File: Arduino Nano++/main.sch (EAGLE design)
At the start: 68 parts, among them IC1 LM358N, Q1 IRF9530, Q2 IRF9530

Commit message: Nano++ schematic; guitar hero redo to not use 1/64th bit
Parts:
- removed 10K, 3.9K, 7.68K: (no value), rcl:R-US_0204/7
- removed ANALOG: (no value), con-lsta:FE08-1
- removed D23, D24, D25: BZX90, diode:BZX90
- removed F21, F22: FUSETE5, fuse:FUSETE5
- added D3: BZX90, diode:BZX90
- added R10: 1k, rcl:R-US_0204/7
- added R8, R9: 300, rcl:R-US_0204/7
- added SV3: (no value), con-lsta:FE06-1
- R2: value 10k -> (none)
- R3: value 300 -> (none)
- R5: value 300 -> 10k
- R6: value 1k -> (none)
- renumbered 7.68K1 to R7, D26 to D2, DC_JACK to J1, DIGITAL_0 to SV5, DIGITAL_1 to SV4, NANO_LEFT to SV6, NANO_RIGHT to SV7, POWER to SV2, VREG to SV1
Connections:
- removed net A6: D20.C, F17.1, SV6.10
- removed net A6': ANALOG.2, F17.2
- removed net A7: D21.C, F18.1, SV6.11
- removed net A7': ANALOG.1, F18.2
- removed net N$1: SV2.8
- net 3V3: now also R5.2; no longer R4.2
- net 3V3': now also R6.2; no longer 3.9K.2
- net 3V3EN: now also R9.2; no longer R5.2
- net 5V: now also R3.1, R4.2; no longer R1.1, R2.2
- net 5V': now also R1.2; no longer 10K.2
- net 5VEN: now also R8.2; no longer R3.2
- net A0: now also D5.C, F3.1; no longer D25.C, F22.1
- net A0': now also F3.2, SV3.6; no longer ANALOG.8, F22.2
- net A1: now also D8.C, F6.1; no longer D24.C, F21.1
- net A1': now also F6.2, SV3.5; no longer ANALOG.7, F21.2
- net A2: now also D11.C, F9.1; no longer D23.C, F20.1
- net A2': now also F9.2, SV3.4; no longer ANALOG.6, F20.2
- net A3: now also D14.C, F12.1; no longer D22.C, F19.1
- net A3': now also F12.2, SV3.3; no longer ANALOG.5, F19.2
- net A4: now also D17.C; no longer D18.C
- net A4': now also SV3.2; no longer ANALOG.4
- net A5: now also D20.C, F18.1; no longer D19.C, F16.1
- net A5': now also F18.2, SV3.1; no longer ANALOG.3, F16.2
- net D0: now also D3.C, F1.1; no longer D11.C, F7.1
- net D0': now also F1.2; no longer F7.2
- net D1: now also D6.C, F4.1; no longer D10.C, F6.1
- net D1': now also F4.2; no longer F6.2
- net D10: now also D10.C, F8.1; no longer D15.C, F12.1
- net D10': now also F8.2; no longer F12.2
- net D11: now also D13.C; no longer D14.C
- net D12: now also D16.C, F14.1; no longer D12.C, F9.1
- net D12': now also F14.2; no longer F9.2
- net D13: now also D19.C, F17.1; no longer D13.C, F10.1
- net D13': now also F17.2; no longer F10.2
- net D2: now also F7.1; no longer F5.1
- net D2': now also F7.2; no longer F5.2
- net D3: now also D12.C, F10.1; no longer D8.C, F4.1
- net D3': now also F10.2; no longer F4.2
- net D4: now also D15.C, F13.1; no longer D5.C, F8.1
- net D4': now also F13.2; no longer F8.2
- net D5: now also D18.C, F16.1; no longer D4.C, F1.1
- net D5': now also F16.2; no longer F1.2
- net D6: now also D21.C, F19.1; no longer D6.C, F2.1
- net D6': now also F19.2; no longer F2.2
- net D7: now also D22.C, F20.1; no longer D7.C, F3.1
- net D7': now also F20.2; no longer F3.2
- net D8: now also D4.C, F2.1; no longer D17.C, F14.1
- net D8': now also F2.2; no longer F14.2
- net D9: now also D7.C, F5.1; no longer D16.C, F13.1
- net D9': now also F5.2; no longer F13.2
- net GND: now also D3.A, R2.1; no longer 7.68K.1, D23.A, D24.A, D25.A
- net N$3: now also R9.1; no longer R4.1
- net N$4: now also R4.1, R8.1; no longer R2.1, R3.1
- net N$6: now also R1.1, R2.2; no longer 10K.1, 7.68K.2
- net N$7: now also R6.1; no longer 3.9K.1
- net RST: now also R10.2; no longer R6.2
- net RST': now also R10.1; no longer R6.1
- net VIN: now also SV6.15
- net VREF2.4: now also R3.2; no longer R1.2
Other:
- moved on the sheet: D10, D11, D12, D13, D14, D15, D16, D17, D18, D19, D20, D21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

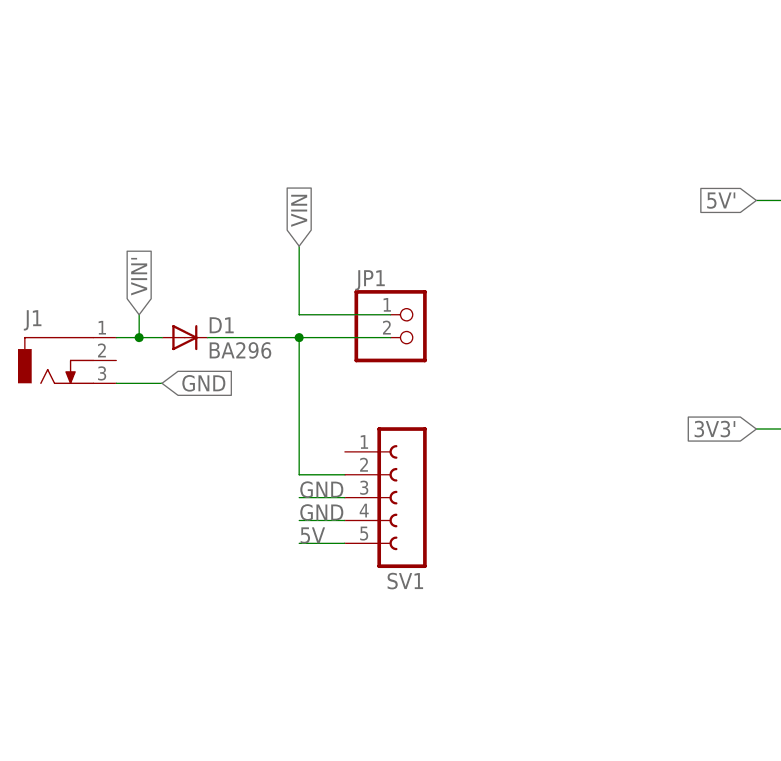
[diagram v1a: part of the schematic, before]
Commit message: Removed vreg slot
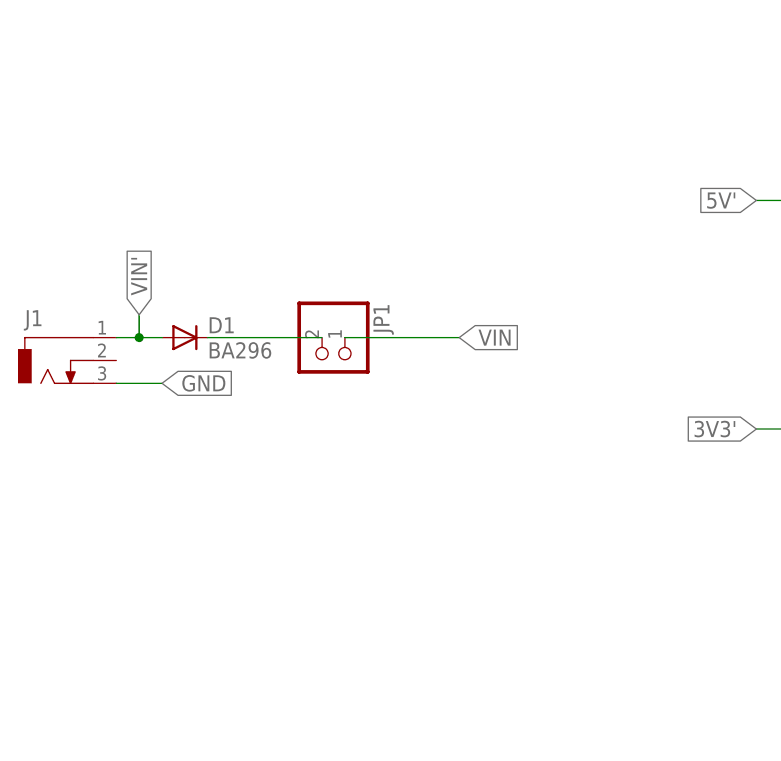
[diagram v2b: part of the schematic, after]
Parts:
- removed SV1: (no value), con-lsta:FE05-1
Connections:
- net 5V: no longer SV1.5
- net GND: no longer SV1.3, SV1.4
- net N$2: no longer SV1.2
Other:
- moved on the sheet: JP1
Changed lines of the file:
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@@
 <part name="SV4" library="con-lsta" library_urn="urn:adsk.eagle:library:161" deviceset="FE08-1" device="" package3d_urn="urn:adsk.eagle:package:8194/1"/>
 <part name="J1" library="con-jack" library_urn="urn:adsk.eagle:library:154" deviceset="DCJ0303" device="" package3d_urn="urn:adsk.eagle:package:7493/1"/>
-<part name="SV1" library="con-lsta" library_urn="urn:adsk.eagle:library:161" deviceset="FE05-1" device="" package3d_urn="urn:adsk.eagle:package:8190/1"/>
 <part name="F13" library="fuse" library_urn="urn:adsk.eagle:library:233" deviceset="FUSE" device="TE5" package3d_urn="urn:adsk.eagle:package:14069/1"/>
 <part name="D15" library="diode" library_urn="urn:adsk.eagle:library:210" deviceset="BZX90" device="" package3d_urn="urn:adsk.eagle:package:43364/1"/>
@@
 <instance part="SV4" gate="G$1" x="121.92" y="25.4" rot="R180"/>
 <instance part="J1" gate="G$1" x="-154.94" y="-40.64"/>
-<instance part="SV1" gate="G$1" x="-114.3" y="-55.88" rot="R180"/>
 <instance part="F13" gate="G$1" x="109.22" y="-55.88" rot="R90"/>
 <instance part="D15" gate="1" x="109.22" y="-68.58" rot="R90"/>
@@
 <instance part="GND4" gate="1" x="-58.42" y="-165.1"/>
 <instance part="D1" gate="1" x="-139.7" y="-38.1"/>
-<instance part="JP1" gate="G$1" x="-114.3" y="-38.1"/>
+<instance part="JP1" gate="G$1" x="-124.46" y="-40.64" rot="R270"/>
 <instance part="R10" gate="G$1" x="-35.56" y="-96.52"/>
 <instance part="SV3" gate="G$1" x="81.28" y="-5.08"/>
@@
 </segment>
 <segment>
-<pinref part="SV1" gate="G$1" pin="5"/>
-<wire x1="-121.92" y1="-60.96" x2="-127" y2="-60.96" width="0.1524" layer="91"/>
-<label x="-127" y="-60.96" size="1.778" layer="95"/>
-</segment>
-<segment>
 <pinref part="IC1" gate="P" pin="V+"/>
 <wire x1="-81.28" y1="-93.98" x2="-81.28" y2="-91.44" width="0.1524" layer="91"/>
@@
 <wire x1="-147.32" y1="-43.18" x2="-142.24" y2="-43.18" width="0.1524" layer="91"/>
 <label x="-142.24" y="-43.18" size="1.778" layer="95" xref="yes"/>
-</segment>
-<segment>
-<pinref part="SV1" gate="G$1" pin="3"/>
-<wire x1="-121.92" y1="-55.88" x2="-127" y2="-55.88" width="0.1524" layer="91"/>
-<label x="-127" y="-55.88" size="1.778" layer="95"/>
-</segment>
-<segment>
-<pinref part="SV1" gate="G$1" pin="4"/>
-<wire x1="-121.92" y1="-58.42" x2="-127" y2="-58.42" width="0.1524" layer="91"/>
-<label x="-127" y="-58.42" size="1.778" layer="95"/>
 </segment>
 </net>
@@
 <segment>
 <pinref part="D1" gate="1" pin="C"/>
-<wire x1="-137.16" y1="-38.1" x2="-127" y2="-38.1" width="0.1524" layer="91"/>
 <pinref part="JP1" gate="G$1" pin="2"/>
-<wire x1="-127" y1="-38.1" x2="-116.84" y2="-38.1" width="0.1524" layer="91"/>
-<junction x="-127" y="-38.1"/>
-<wire x1="-127" y1="-38.1" x2="-127" y2="-53.34" width="0.1524" layer="91"/>
-<pinref part="SV1" gate="G$1" pin="2"/>
-<wire x1="-127" y1="-53.34" x2="-121.92" y2="-53.34" width="0.1524" layer="91"/>
+<wire x1="-137.16" y1="-38.1" x2="-124.46" y2="-38.1" width="0.1524" layer="91"/>
 </segment>
 </net>
@@
 <segment>
 <pinref part="JP1" gate="G$1" pin="1"/>
-<wire x1="-116.84" y1="-35.56" x2="-127" y2="-35.56" width="0.1524" layer="91"/>
-<wire x1="-127" y1="-35.56" x2="-127" y2="-27.94" width="0.1524" layer="91"/>
-<label x="-127" y="-27.94" size="1.778" layer="95" rot="R90" xref="yes"/>
-</segment>
-<segment>
+<wire x1="-121.92" y1="-38.1" x2="-109.22" y2="-38.1" width="0.1524" layer="91"/>
+<label x="-109.22" y="-38.1" size="1.778" layer="95" xref="yes"/>
+</segment>
+<segment>
